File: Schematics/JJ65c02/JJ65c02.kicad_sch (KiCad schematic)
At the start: 29 parts, among them SW1 RESET, U1 74HC00, U2 NE555, U3 74HC00

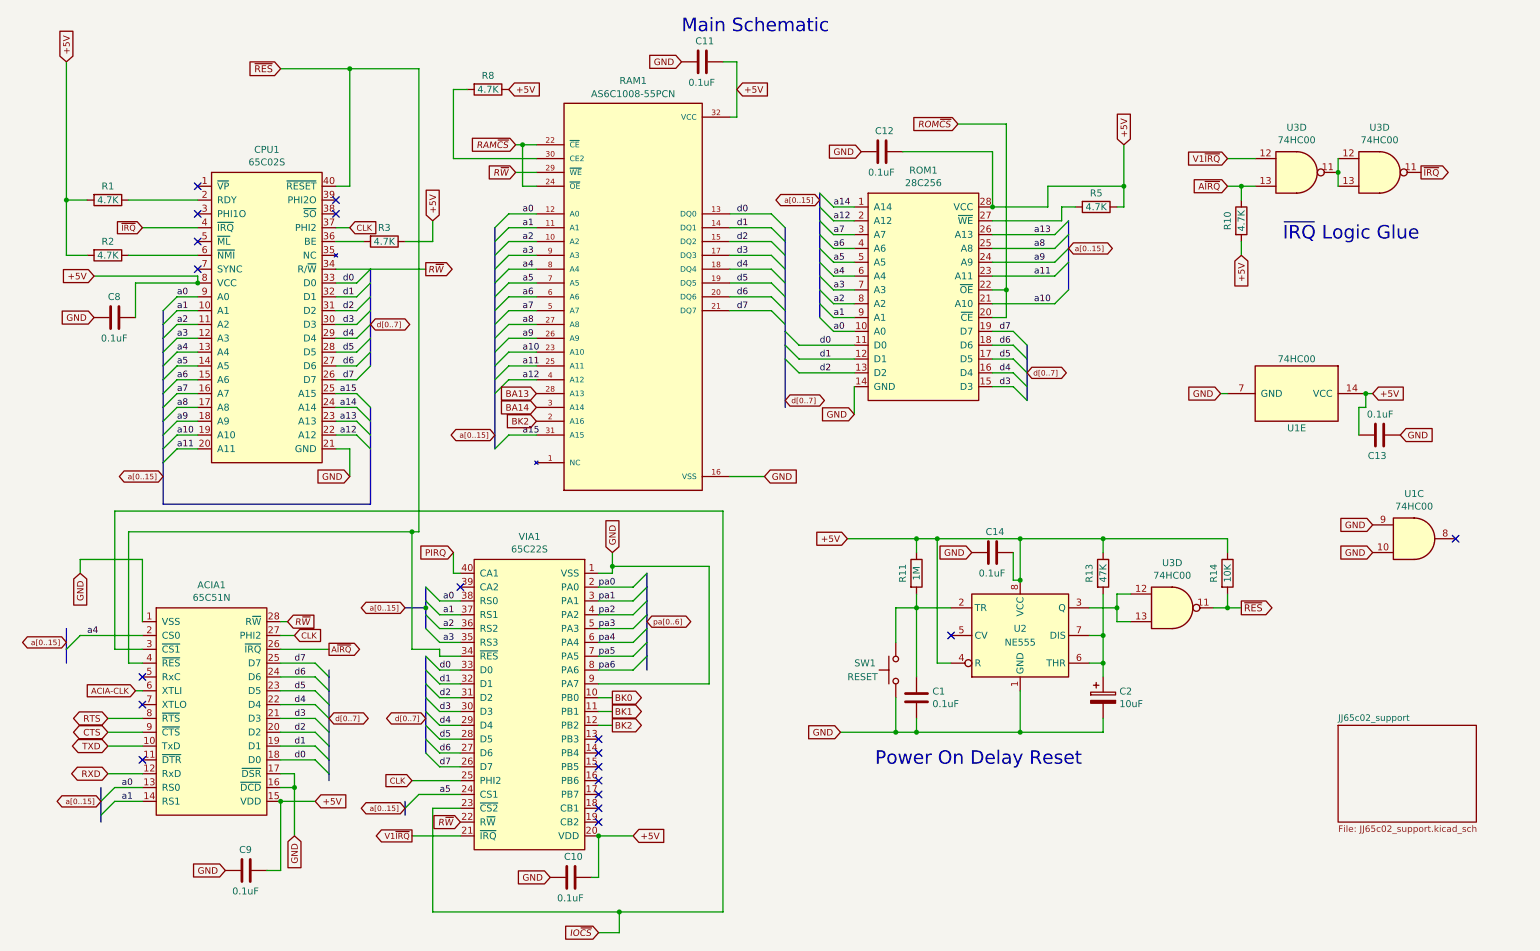
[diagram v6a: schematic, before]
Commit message: Updated schematics for v2-pico
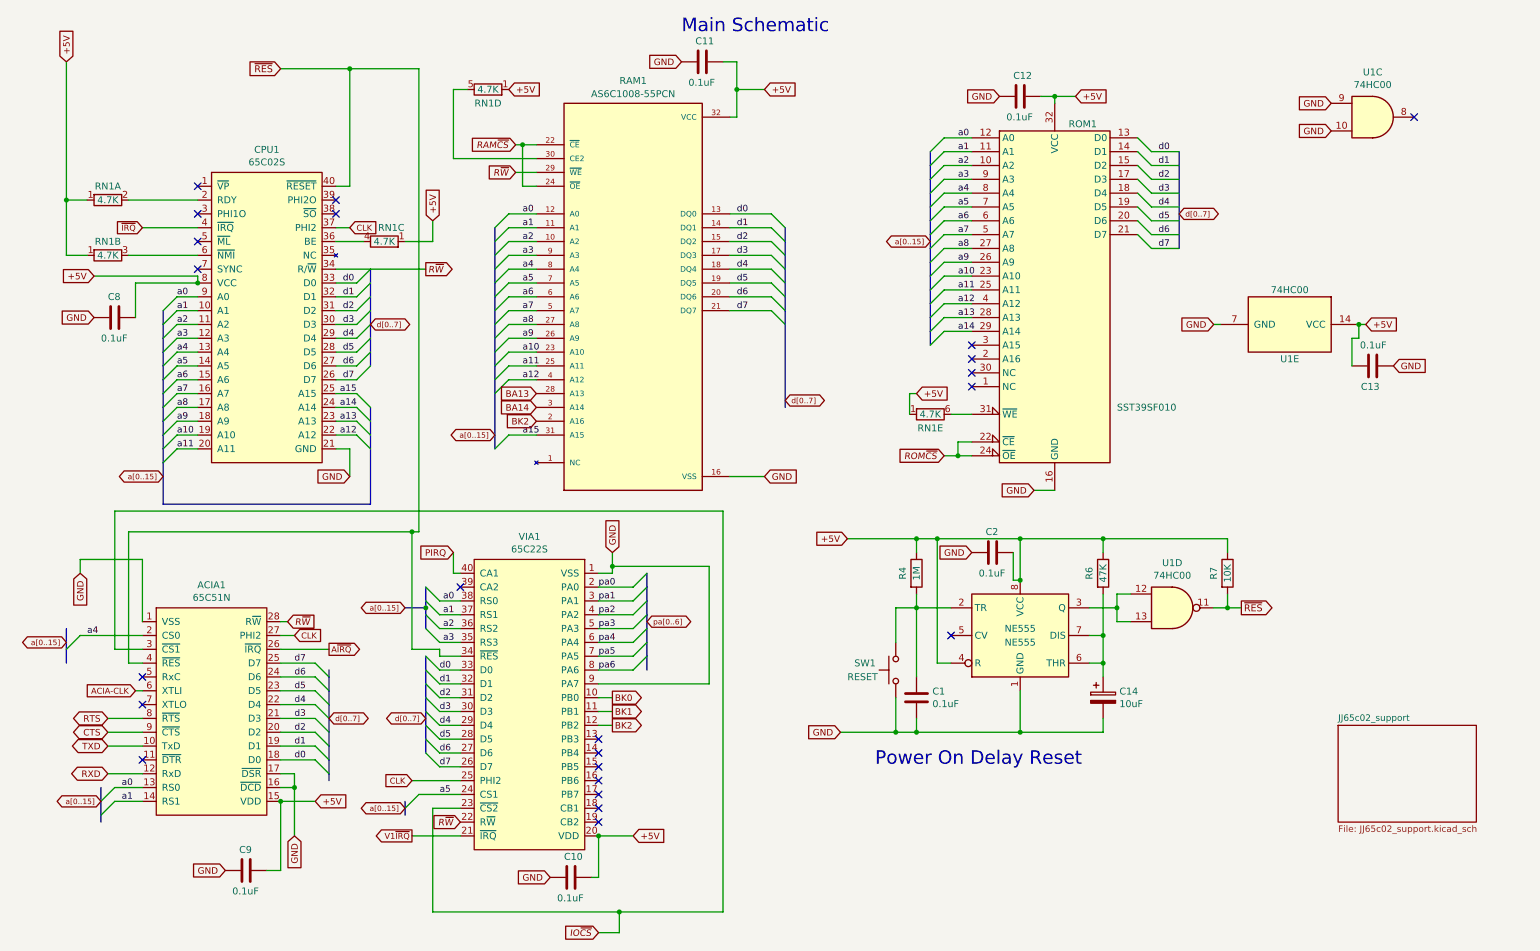
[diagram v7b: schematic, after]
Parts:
- removed R1, R10, R2, R3, R5, R8: 4.7K, Resistor_THT:R_Axial_DIN0207_L6.3mm_D2.5mm_P7.62mm_Horizontal, symbol Device:R
- removed ROM1: 28C256, Package_DIP:DIP-28_W15.24mm_Socket, symbol 6502:28C256
- removed U3 (x2): 74HC00, Package_DIP:DIP-14_W7.62mm_Socket, symbol 74xx:74HC00
- added RN1: 4.7K, Resistor_THT:R_Array_SIP6, symbol Device:R_Network06_Split
- added ROM1: SST39SF010, Package_DIP:DIP-32_W15.24mm_Socket, symbol Memory_Flash:SST39SF010
- renumbered C2 to C14, C14 to C2, U2 to NE555, R11 to R4, R13 to R6, R14 to R7, U3 to U1
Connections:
- net +5V: now also RN1.1 (R1), RN1.1 (R1), RN1.1 (R1), RN1.1 (R1), RN1.1 (R1), ROM1.32 (VCC)
- net GND: now also ROM1.16 (GND)
- net ROM~{CS}: now also ROM1.22 (~{CE}), ROM1.24 (~{OE})
- net a0: now also ROM1.12 (A0)
- net a1: now also ROM1.11 (A1)
- net a10: now also ROM1.23 (A10)
- net a11: now also ROM1.25 (A11)
- net a12: now also ROM1.4 (A12)
- net a13: now also ROM1.28 (A13)
- net a14: now also ROM1.29 (A14)
- net a2: now also ROM1.10 (A2)
- net a3: now also ROM1.9 (A3)
- net a4: now also ROM1.8 (A4)
- net a5: now also ROM1.7 (A5)
- net a6: now also ROM1.6 (A6)
- net a7: now also ROM1.5 (A7)
- net a8: now also ROM1.27 (A8)
- net a9: now also ROM1.26 (A9)
- net at CPU1.2 (RDY): now also RN1.2 (R1.2)
- net at CPU1.36 (BE): now also RN1.4 (R3.2)
- net at CPU1.6 (~{NMI}): now also RN1.3 (R2.2)
- net at RAM1.30 (CE2): now also RN1.5 (R4.2)
- new net: RN1.6 (R5.2), ROM1.31 (~{WE})
- no-connect marks 19 -> 23
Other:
- note removed: "~{IRQ} Logic Glue"
- moved on the sheet: C12, C13, U1C, U1E

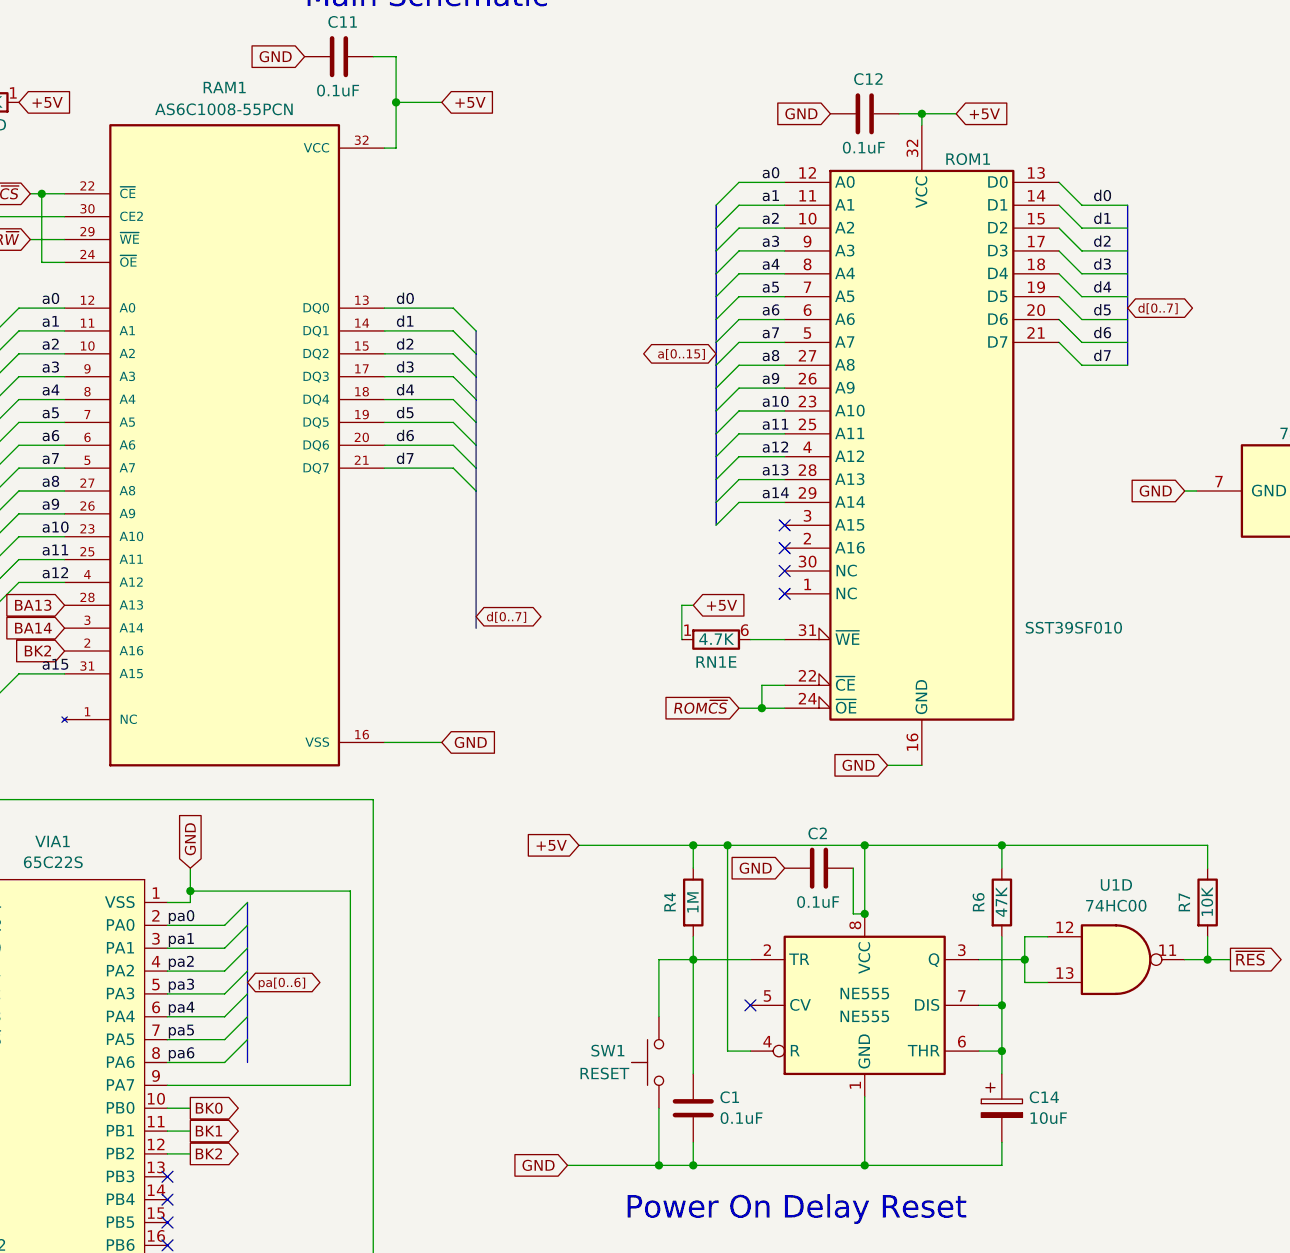
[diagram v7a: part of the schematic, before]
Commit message: if we are using the pi pico to generate the clock, we need to level convert from 3.3 to 5v
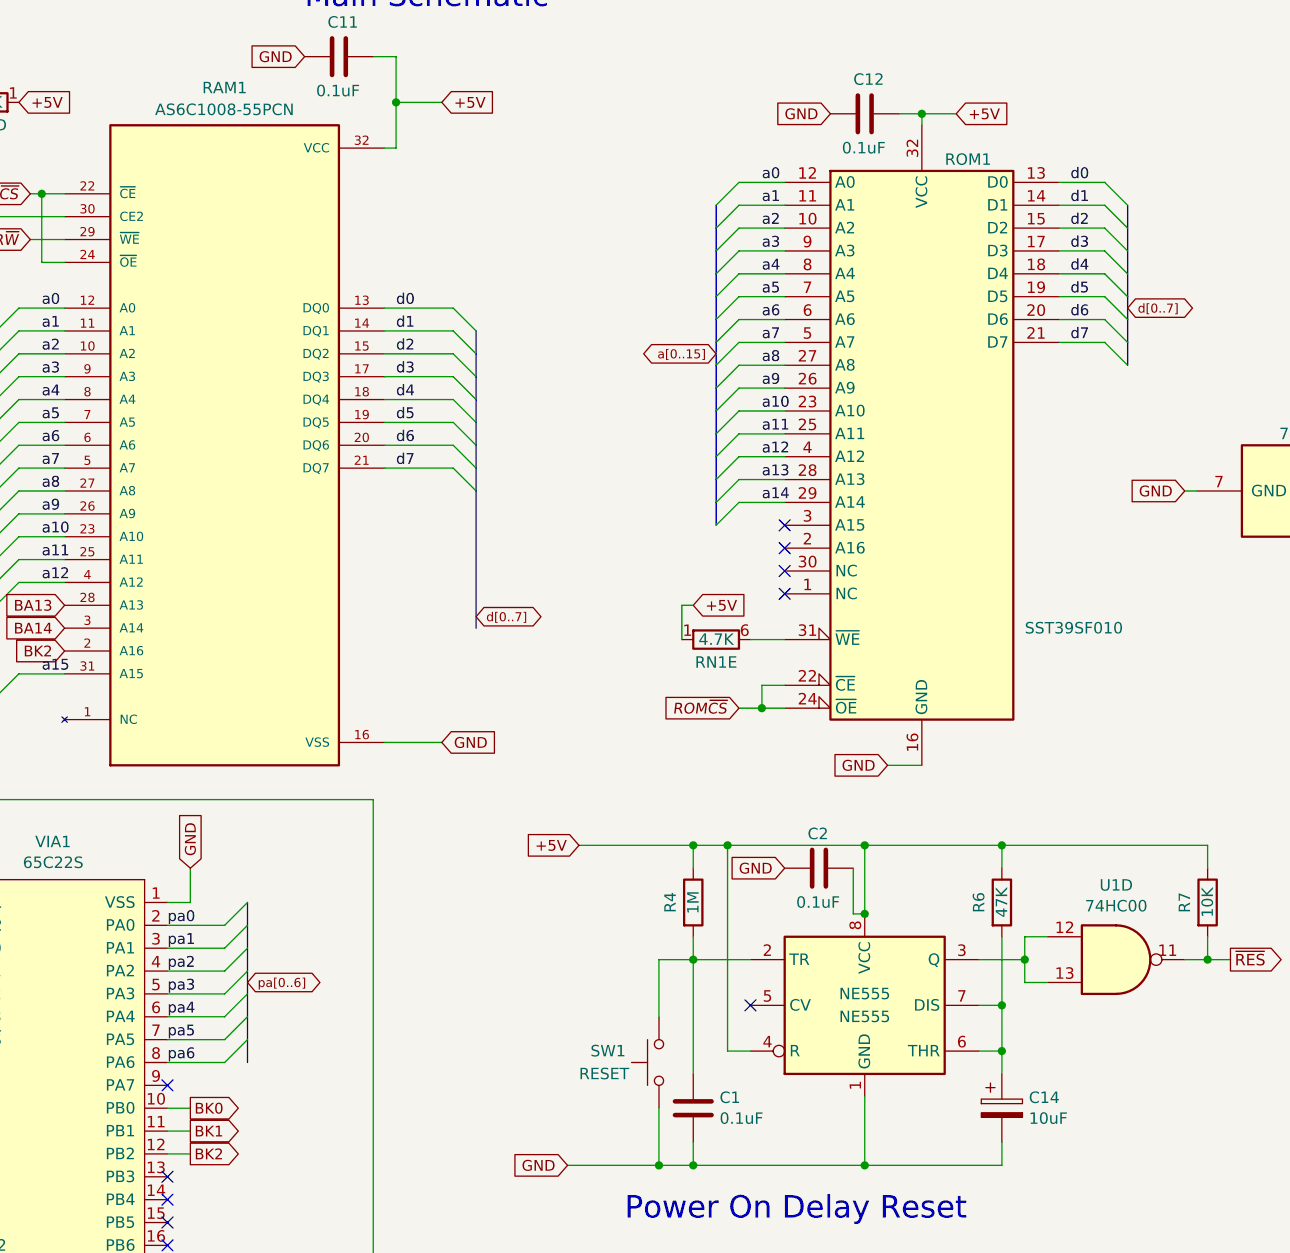
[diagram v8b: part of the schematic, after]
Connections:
- net GND: no longer VIA1.9 (PA7)
- net d0: now also ROM1.13 (D0)
- net d1: now also ROM1.14 (D1)
- net d2: now also ROM1.15 (D2)
- net d3: now also ROM1.17 (D3)
- net d4: now also ROM1.18 (D4)
- net d5: now also ROM1.19 (D5)
- net d6: now also ROM1.20 (D6)
- net d7: now also ROM1.21 (D7)
- no-connect marks 23 -> 24
